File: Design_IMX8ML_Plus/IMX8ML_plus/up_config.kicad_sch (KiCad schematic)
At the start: 5 parts, among them U1 MIMX8ML8CVNKZAB, Y2 24MHz

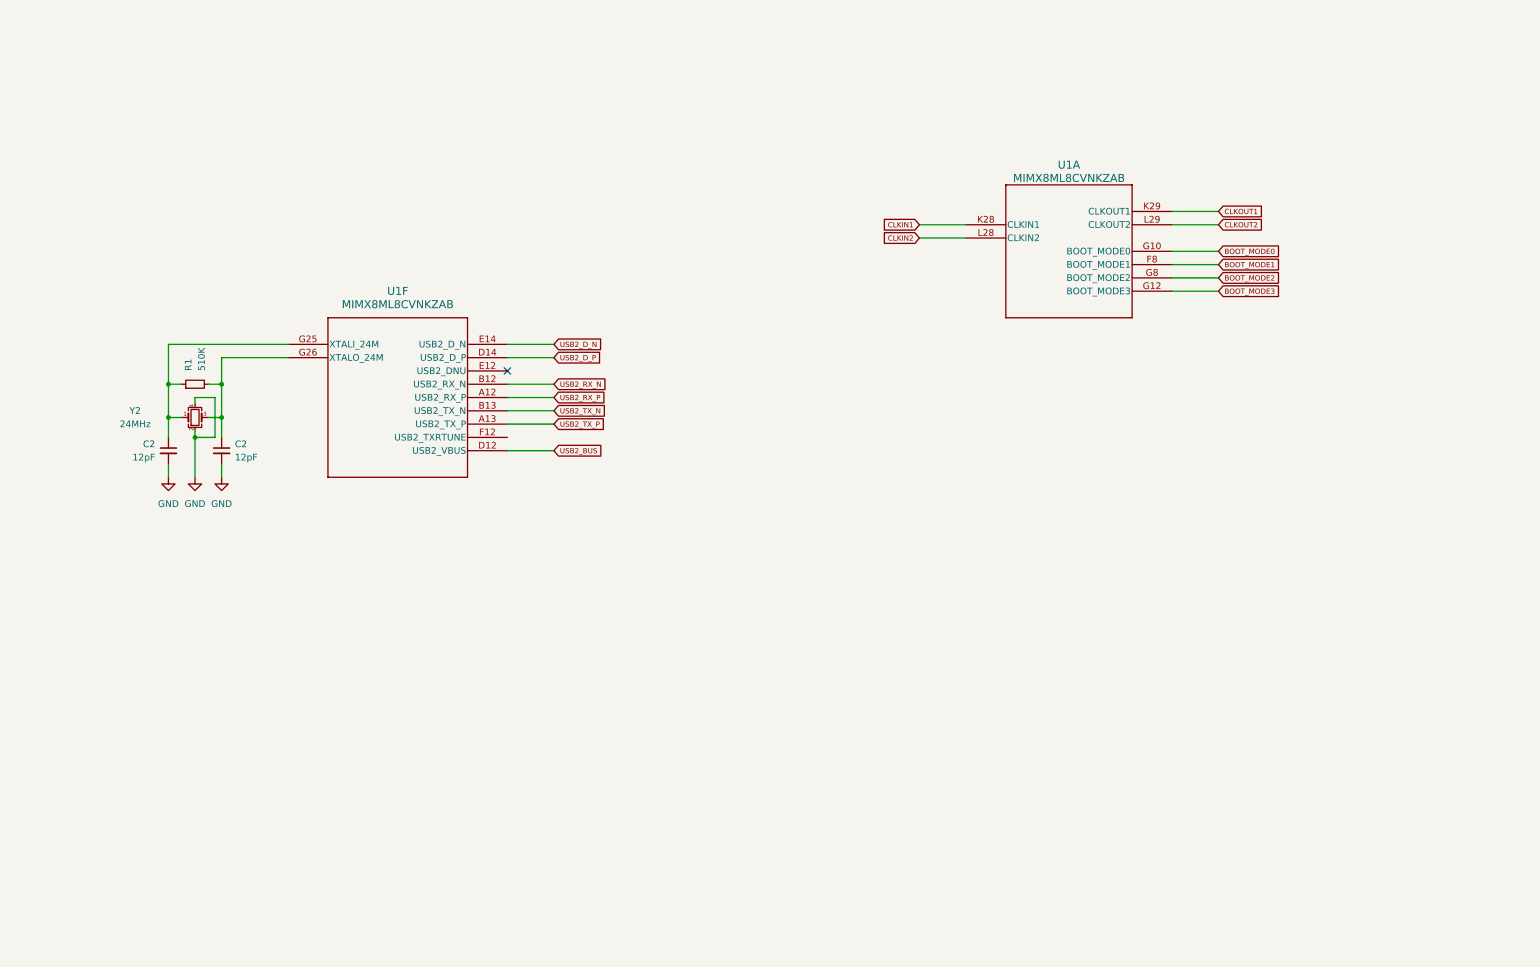
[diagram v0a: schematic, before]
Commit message: Update schematic and add ethernet interface ksz9131rn
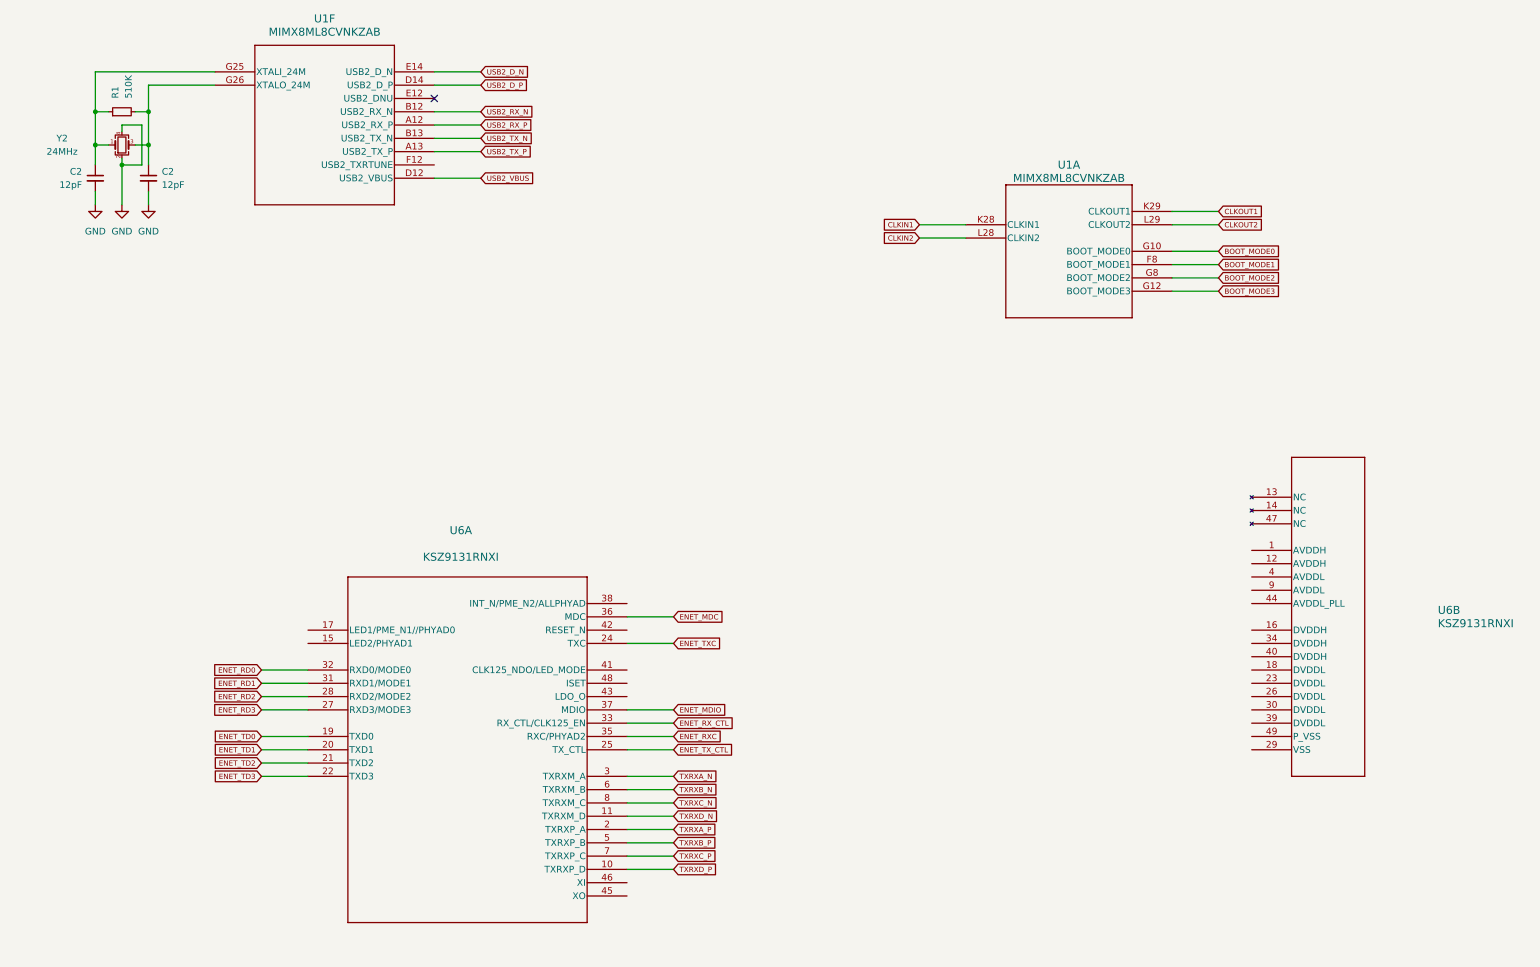
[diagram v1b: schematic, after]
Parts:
- added U6: KSZ9131RNXI, Package_DFN_QFN:QFN-48-1EP_7x7mm_P0.5mm_EP5.6x5.6mm, symbol KSZ9131RNXI:KSZ9131RNXI
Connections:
- net USB2_BUS renamed USB2_VBUS
- new net ENET_MDC: U6.36 (MDC)
- new net ENET_MDIO: U6.37 (MDIO)
- new net ENET_RD0: U6.32 (RXD0/MODE0)
- new net ENET_RD1: U6.31 (RXD1/MODE1)
- new net ENET_RD2: U6.28 (RXD2/MODE2)
- new net ENET_RD3: U6.27 (RXD3/MODE3)
- new net ENET_RXC: U6.35 (RXC/PHYAD2)
- new net ENET_RX_CTL: U6.33 (RX_CTL/CLK125_EN)
- new net ENET_TD0: U6.19 (TXD0)
- new net ENET_TD1: U6.20 (TXD1)
- new net ENET_TD2: U6.21 (TXD2)
- new net ENET_TD3: U6.22 (TXD3)
- new net ENET_TXC: U6.24 (TXC)
- new net ENET_TX_CTL: U6.25 (TX_CTL)
- new net TXRXA_N: U6.3 (TXRXM_A)
- new net TXRXA_P: U6.2 (TXRXP_A)
- new net TXRXB_N: U6.6 (TXRXM_B)
- new net TXRXB_P: U6.5 (TXRXP_B)
- new net TXRXC_N: U6.8 (TXRXM_C)
- new net TXRXC_P: U6.7 (TXRXP_C)
- new net TXRXD_N: U6.11 (TXRXM_D)
- new net TXRXD_P: U6.10 (TXRXP_D)
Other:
- moved on the sheet: C2, R1, U1F, Y2

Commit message: Add power layer
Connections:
- net GND: now also U6.29 (VSS), U6.49 (P_VSS)
- net at U6.16 (DVDDH): now also U6.34 (DVDDH), U6.40 (DVDDH)
- net at U6.18 (DVDDL): now also U6.23 (DVDDL), U6.26 (DVDDL), U6.30 (DVDDL), U6.39 (DVDDL)
- net LED2: now reaches U6.15 (LED2/PHYAD1)
- net LED1: now reaches U6.17 (LED1/PME_N1//PHYAD0)
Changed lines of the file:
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@@
 (kicad_sch (version 20230121) (generator eeschema)
   (paper "A4")
+  (junction (at 251.46 134.62) (diameter 0) (color 0 0 0 0)
+  )
   (junction (at 39.37 43.18) (diameter 0) (color 0 0 0 0)
   )
+  (junction (at 251.46 147.32) (diameter 0) (color 0 0 0 0)
+  )
+  (junction (at 251.46 144.78) (diameter 0) (color 0 0 0 0)
+  )
+  (junction (at 251.46 154.94) (diameter 0) (color 0 0 0 0)
+  )
   (junction (at 44.45 39.37) (diameter 0) (color 0 0 0 0)
   )
@@
   (junction (at 34.29 39.37) (diameter 0) (color 0 0 0 0)
   )
+  (junction (at 251.46 142.24) (diameter 0) (color 0 0 0 0)
+  )
   (junction (at 44.45 33.02) (diameter 0) (color 0 0 0 0)
   )
   (no_connect (at 99.06 30.48))
+  (wire (pts (xy 251.46 147.32) (xy 251.46 149.86))
+    (stroke (width 0) (type default))
+  )
   (wire (pts (xy 99.06 38.1) (xy 107.95 38.1))
     (stroke (width 0) (type default))
@@
     (stroke (width 0) (type default))
   )
+  (wire (pts (xy 255.27 139.7) (xy 251.46 139.7))
+    (stroke (width 0) (type default))
+  )
   (wire (pts (xy 39.37 43.18) (xy 39.37 50.8))
     (stroke (width 0) (type default))
   )
+  (wire (pts (xy 74.93 132.08) (xy 66.04 132.08))
+    (stroke (width 0) (type default))
+  )
   (wire (pts (xy 135.89 152.4) (xy 144.78 152.4))
     (stroke (width 0) (type default))
@@
     (stroke (width 0) (type default))
   )
+  (wire (pts (xy 251.46 144.78) (xy 255.27 144.78))
+    (stroke (width 0) (type default))
+  )
   (wire (pts (xy 74.93 160.02) (xy 66.04 160.02))
     (stroke (width 0) (type default))
@@
     (stroke (width 0) (type default))
   )
+  (wire (pts (xy 251.46 147.32) (xy 255.27 147.32))
+    (stroke (width 0) (type default))
+  )
+  (wire (pts (xy 255.27 152.4) (xy 251.46 152.4))
+    (stroke (width 0) (type default))
+  )
   (wire (pts (xy 135.89 134.62) (xy 144.78 134.62))
     (stroke (width 0) (type default))
@@
     (stroke (width 0) (type default))
   )
+  (wire (pts (xy 251.46 154.94) (xy 255.27 154.94))
+    (stroke (width 0) (type default))
+  )
   (wire (pts (xy 74.93 147.32) (xy 66.04 147.32))
     (stroke (width 0) (type default))
@@
     (stroke (width 0) (type default))
   )
+  (wire (pts (xy 251.46 132.08) (xy 255.27 132.08))
+    (stroke (width 0) (type default))
+  )
   (wire (pts (xy 240.03 59.69) (xy 248.92 59.69))
     (stroke (width 0) (type default))
@@
     (stroke (width 0) (type default))
   )
+  (wire (pts (xy 74.93 134.62) (xy 66.04 134.62))
+    (stroke (width 0) (type default))
+  )
   (wire (pts (xy 135.89 175.26) (xy 144.78 175.26))
     (stroke (width 0) (type default))
@@
     (stroke (width 0) (type default))
   )
+  (wire (pts (xy 251.46 134.62) (xy 255.27 134.62))
+    (stroke (width 0) (type default))
+  )
   (wire (pts (xy 44.45 48.26) (xy 44.45 50.8))
     (stroke (width 0) (type default))
@@
     (stroke (width 0) (type default))
   )
+  (wire (pts (xy 251.46 142.24) (xy 255.27 142.24))
+    (stroke (width 0) (type default))
+  )
   (wire (pts (xy 135.89 162.56) (xy 144.78 162.56))
     (stroke (width 0) (type default))
@@
     (stroke (width 0) (type default))
   )
+  (wire (pts (xy 251.46 154.94) (xy 251.46 160.02))
+    (stroke (width 0) (type default))
+  )
   (wire (pts (xy 44.45 39.37) (xy 44.45 43.18))
     (stroke (width 0) (type default))
@@
     (stroke (width 0) (type default))
   )
+  (wire (pts (xy 255.27 137.16) (xy 251.46 137.16))
+    (stroke (width 0) (type default))
+  )
   (wire (pts (xy 135.89 172.72) (xy 144.78 172.72))
     (stroke (width 0) (type default))
@@
     (stroke (width 0) (type default))
   )
+  (wire (pts (xy 251.46 149.86) (xy 255.27 149.86))
+    (stroke (width 0) (type default))
+  )
   (wire (pts (xy 44.45 39.37) (xy 44.45 33.02))
     (stroke (width 0) (type default))
@@
     (stroke (width 0) (type default))
   )
+  (wire (pts (xy 251.46 152.4) (xy 251.46 154.94))
+    (stroke (width 0) (type default))
+  )
+  (wire (pts (xy 251.46 134.62) (xy 251.46 132.08))
+    (stroke (width 0) (type default))
+  )
   (wire (pts (xy 99.06 25.4) (xy 107.95 25.4))
     (stroke (width 0) (type default))
   )
+  (wire (pts (xy 251.46 142.24) (xy 251.46 144.78))
+    (stroke (width 0) (type default))
+  )
+  (wire (pts (xy 251.46 137.16) (xy 251.46 134.62))
+    (stroke (width 0) (type default))
+  )
   (wire (pts (xy 74.93 139.7) (xy 66.04 139.7))
     (stroke (width 0) (type default))
@@
     (stroke (width 0) (type default))
   )
+  (wire (pts (xy 251.46 144.78) (xy 251.46 147.32))
+    (stroke (width 0) (type default))
+  )
+  (wire (pts (xy 251.46 139.7) (xy 251.46 142.24))
+    (stroke (width 0) (type default))
+  )
   (wire (pts (xy 39.37 43.18) (xy 43.18 43.18))
     (stroke (width 0) (type default))
@@
   (wire (pts (xy 240.03 62.23) (xy 248.92 62.23))
     (stroke (width 0) (type default))
+  )
+  (global_label "LED1" (shape input) (at 66.04 132.08 180) (fields_autoplaced)
+    (effects (font (size 1 1)) (justify right))
+    (property "Intersheetrefs" "${INTERSHEET_REFS}" (at 60.0854 132.08 0)
+      (effects (font (size 1.27 1.27)) (justify right) hide)
+    )
   )
   (global_label "ENET_TX_CTL" (shape input) (at 144.78 154.94 0) (fields_autoplaced)
@@
     (property "Intersheetrefs" "${INTERSHEET_REFS}" (at 153.4012 160.02 0)
       (effects (font (size 1.27 1.27)) (justify left) hide)
+    )
+  )
+  (global_label "LED2" (shape input) (at 66.04 134.62 180) (fields_autoplaced)
+    (effects (font (size 1 1)) (justify right))
+    (property "Intersheetrefs" "${INTERSHEET_REFS}" (at 60.0854 134.62 0)
+      (effects (font (size 1.27 1.27)) (justify right) hide)
     )
   )
@@
         )
       )
+    )
+  )
+  (symbol (lib_id "power:GND") (at 251.46 160.02 0) (unit 1)
+    (in_bom yes) (on_board yes) (dnp no) (fields_autoplaced)
+    (property "Reference" "#PWR05" (at 251.46 166.37 0)
+      (effects (font (size 1.27 1.27)) hide)
+    )
+    (property "Value" "GND" (at 251.46 165.1 0)
+      (effects (font (size 1.27 1.27)))
+    )
+    (property "Footprint" "" (at 251.46 160.02 0)
+      (effects (font (size 1.27 1.27)) hide)
+    )
+    (property "Datasheet" "" (at 251.46 160.02 0)
+      (effects (font (size 1.27 1.27)) hide)
+    )
+    (pin "1")
+    (instances
+      (project "IMX8ML_plus"
+        (path "/1e0dca60-79b3-4b5b-ab8f-7b2adbc68a5f/c2b8be6d-439a-444c-a168-f4e9f22d3fc9/17e995b4-9d0e-4742-bc8a-27c457a1136a"
+          (reference "#PWR05") (unit 1)
+        )
+      )

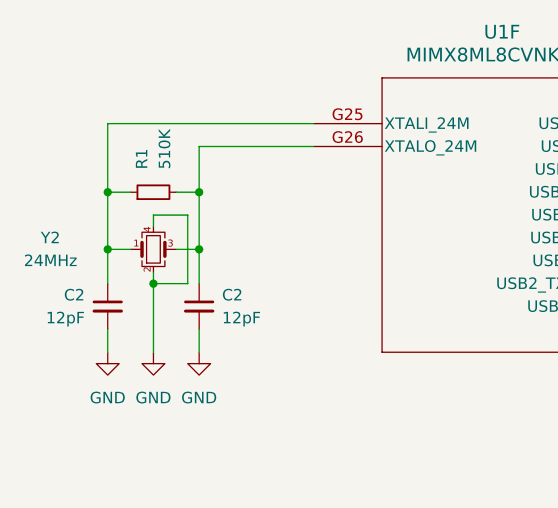
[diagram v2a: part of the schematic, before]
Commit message: Add SPB228 WIFI/BLE module
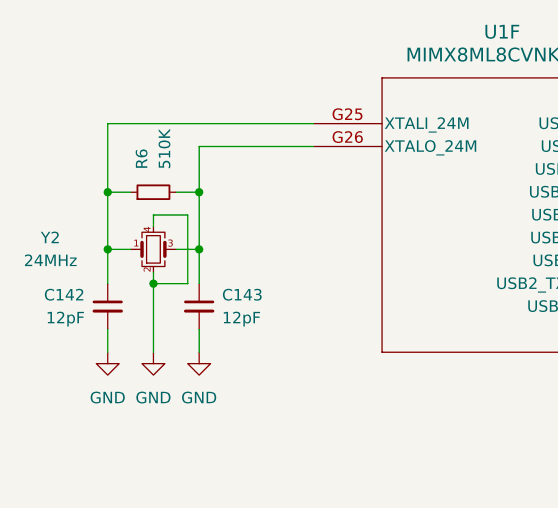
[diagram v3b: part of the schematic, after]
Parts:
- renumbered C2 to C142, C2 to C143, R1 to R6
